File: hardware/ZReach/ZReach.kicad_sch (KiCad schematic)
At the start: 54 parts, among them J1 USB_C_Receptacle_USB2.0, J2 Conn_02x05_Odd_Even, J3 SMA, J4 NM, J5 Qwiic_RA, J6 Conn_01x02, J7 Conn_01x05, J8 Conn_01x05, SW1 PTS810, U1 CP2102N-Axx-xQFN20, U2 EFR32xG23-QFN48, U3 AP2127K-3.3, Y1 39MHz 10ppm, Y2 32768Hz

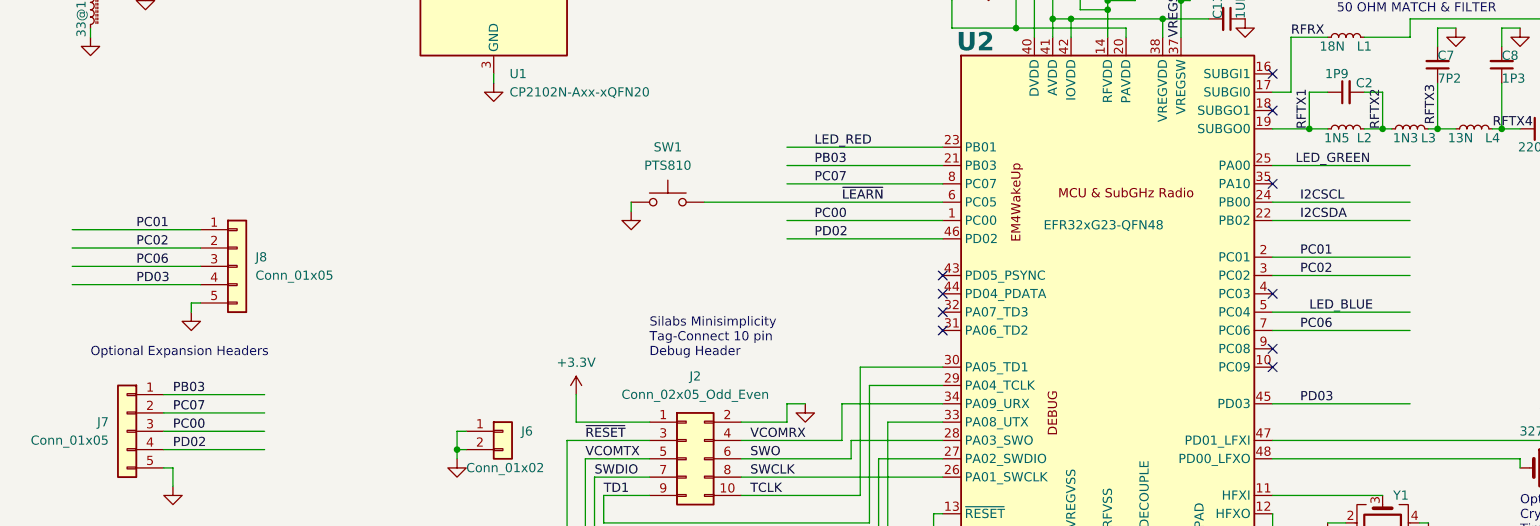
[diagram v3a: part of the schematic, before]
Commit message: PCB Layout DRC clean but needs more cleanup
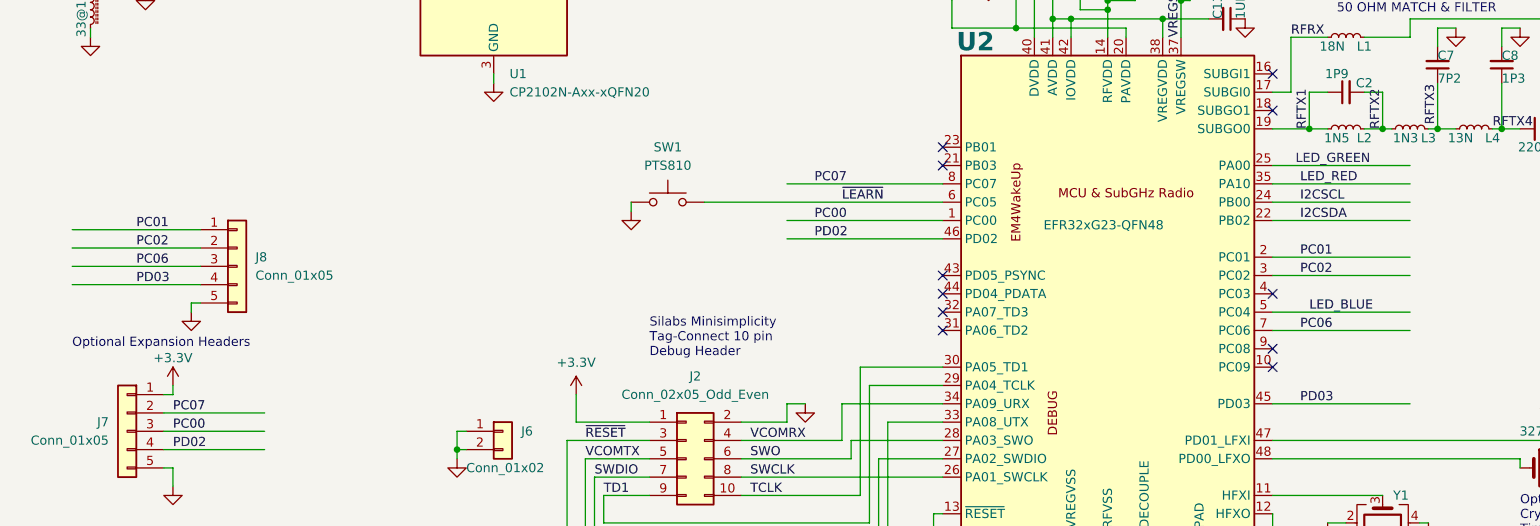
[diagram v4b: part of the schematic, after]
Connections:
- net +3.3V: now also J7.1 (Pin_1)
- net LED_RED: now also U2.35 (PA10); no longer U2.23 (PB01)
- net PB03: no longer names the net of U2.21 (PB03)
- net PB03: no longer J7.1 (Pin_1)
- no-connect marks 21 -> 22
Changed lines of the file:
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@@
   (no_connect (at 53.34 66.04))
   (no_connect (at 99.06 45.72))
+  (no_connect (at 148.59 99.06))
   (no_connect (at 148.59 121.92))
-  (no_connect (at 194.31 104.14))
   (no_connect (at 148.59 119.38))
   (no_connect (at 99.06 60.96))
@@
   (no_connect (at 99.06 73.66))
   (no_connect (at 148.59 116.84))
+  (no_connect (at 148.59 101.6))
   (no_connect (at 194.31 93.98))
   (no_connect (at 99.06 76.2))
@@
     (stroke (width 0) (type default))
   )
-  (wire (pts (xy 127 99.06) (xy 148.59 99.06))
-    (stroke (width 0) (type default))
-  )
   (wire (pts (xy 201.93 151.13) (xy 204.47 151.13))
     (stroke (width 0) (type default))
   )
-  (wire (pts (xy 127 101.6) (xy 148.59 101.6))
-    (stroke (width 0) (type default))
-  )
   (wire (pts (xy 35.56 176.53) (xy 33.02 176.53))
     (stroke (width 0) (type default))
@@
     (stroke (width 0) (type default))
   )
-  (wire (pts (xy 40.64 133.35) (xy 54.61 133.35))
-    (stroke (width 0) (type default))
-  )
   (wire (pts (xy 226.06 90.17) (xy 226.06 96.52))
     (stroke (width 0) (type default))
@@
     (stroke (width 0) (type default))
   )
+  (wire (pts (xy 41.91 133.35) (xy 41.91 132.08))
+    (stroke (width 0) (type default))
+  )
   (wire (pts (xy 90.17 21.59) (xy 86.36 21.59))
     (stroke (width 0) (type default))
@@
     (stroke (width 0) (type default))
   )
+  (wire (pts (xy 40.64 133.35) (xy 41.91 133.35))
+    (stroke (width 0) (type default))
+  )
   (wire (pts (xy 63.5 71.12) (xy 63.5 72.39))
     (stroke (width 0) (type default))
@@
   )
   (wire (pts (xy 196.85 83.82) (xy 196.85 91.44))
+    (stroke (width 0) (type default))
+  )
+  (wire (pts (xy 194.31 104.14) (xy 213.36 104.14))
     (stroke (width 0) (type default))
   )
@@
     (effects (font (size 1.27 1.27)) (justify left bottom))
   )
-  (text "Optional Expansion Headers" (at 30.48 128.27 0)
+  (text "Optional Expansion Headers" (at 27.94 127 0)
     (effects (font (size 1.27 1.27)) (justify left bottom))
   )
@@
     (effects (font (size 1.27 1.27)) (justify left bottom))
   )
-  (label "LED_RED" (at 130.81 99.06 0) (fields_autoplaced)
+  (label "LED_RED" (at 198.12 104.14 0) (fields_autoplaced)
     (effects (font (size 1.27 1.27)) (justify left bottom))
   )
@@
     (effects (font (size 1.27 1.27)) (justify left bottom))
   )
-  (label "PB03" (at 130.81 101.6 0) (fields_autoplaced)
-    (effects (font (size 1.27 1.27)) (justify left bottom))
-  )
   (label "SWDIO" (at 100.33 144.78 0) (fields_autoplaced)
     (effects (font (size 1.27 1.27)) (justify left bottom))
   )
   (label "I2CSCL" (at 198.12 106.68 0) (fields_autoplaced)
-    (effects (font (size 1.27 1.27)) (justify left bottom))
-  )
-  (label "PB03" (at 41.91 133.35 0) (fields_autoplaced)
     (effects (font (size 1.27 1.27)) (justify left bottom))
   )
@@
         )
       )
+    )
+  )
+  (symbol (lib_name "+3.3V_4") (lib_id "power:+3.3V") (at 41.91 132.08 0) (unit 1)
+    (in_bom yes) (on_board yes) (dnp no)
+    (property "Reference" "#PWR042" (at 41.91 135.89 0)
+      (effects (font (size 1.27 1.27)) hide)
+    )
+    (property "Value" "+3.3V" (at 41.91 128.27 0)
+      (effects (font (size 1.27 1.27)))
+    )
+    (property "Footprint" "" (at 41.91 132.08 0)
+      (effects (font (size 1.27 1.27)) hide)
+    )
+    (property "Datasheet" "" (at 41.91 132.08 0)
+      (effects (font (size 1.27 1.27)) hide)
+    )
+    (pin "1")
+    (instances
+      (project "ZReach"
+        (path "/ba492aef-b6eb-4439-8867-b040ec48a543"
+          (reference "#PWR042") (unit 1)
+        )
+      )

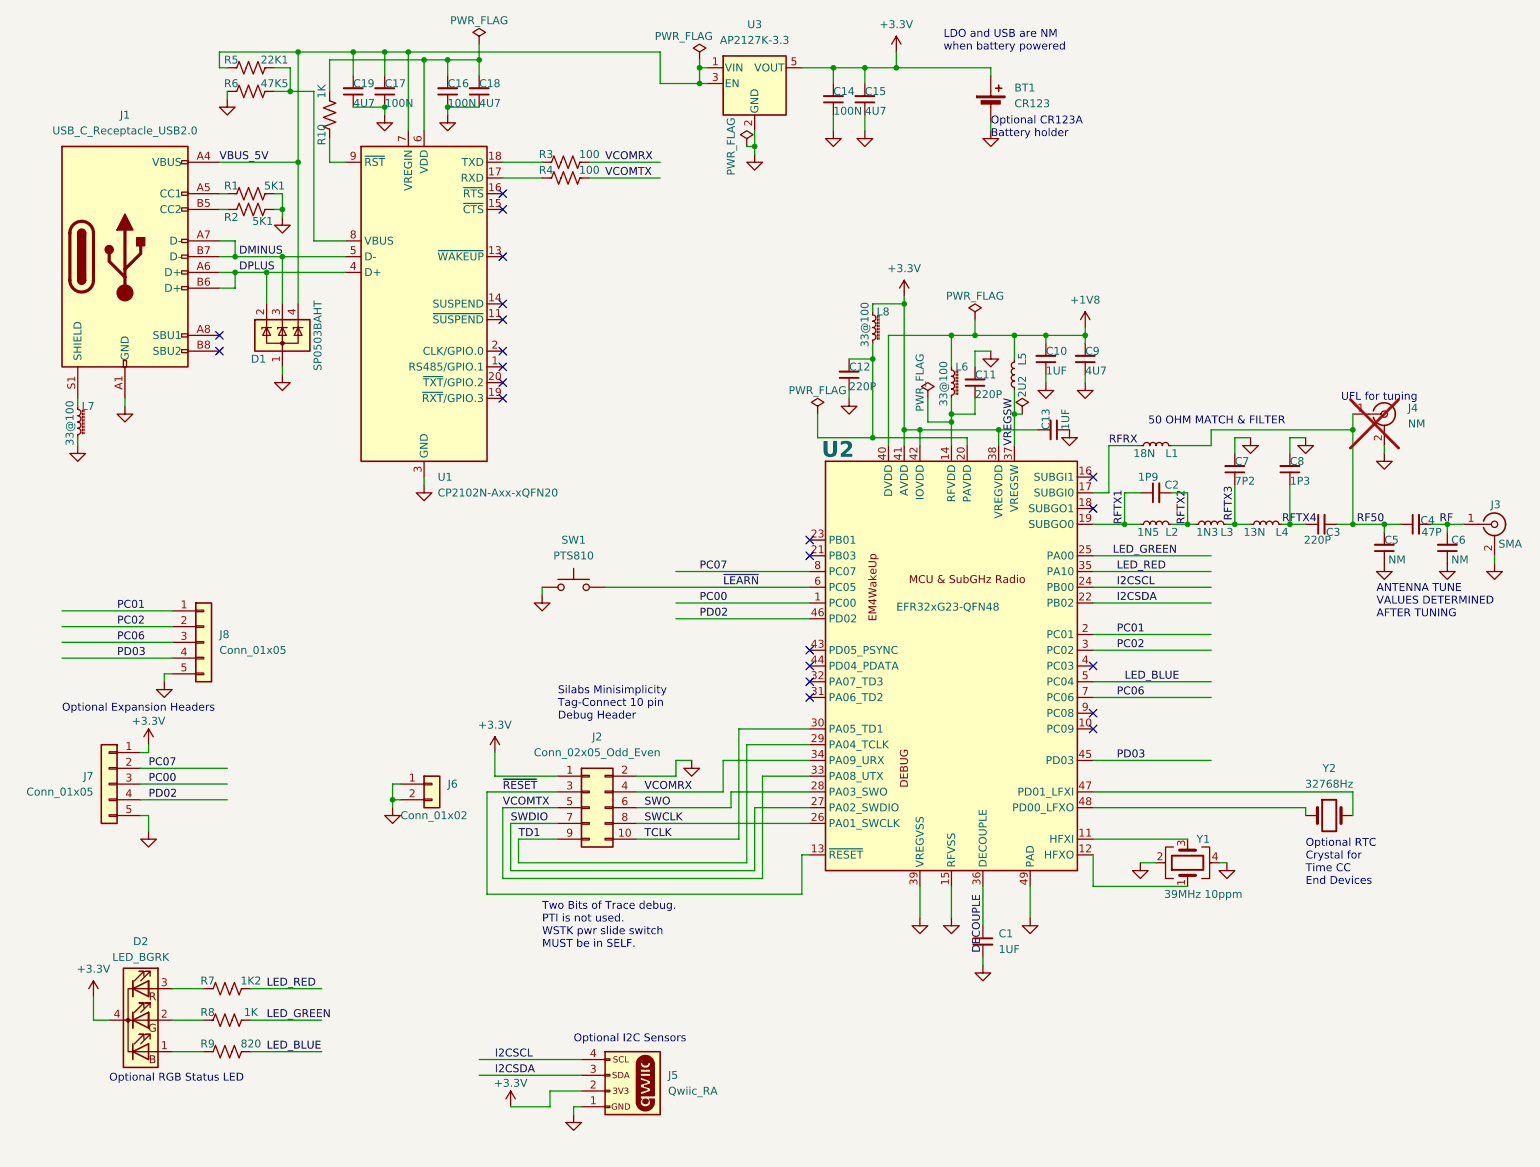
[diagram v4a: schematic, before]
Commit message: Update ZG23 symbol to the official one in the KiCAD library. Updated to KiCAD to V8.0
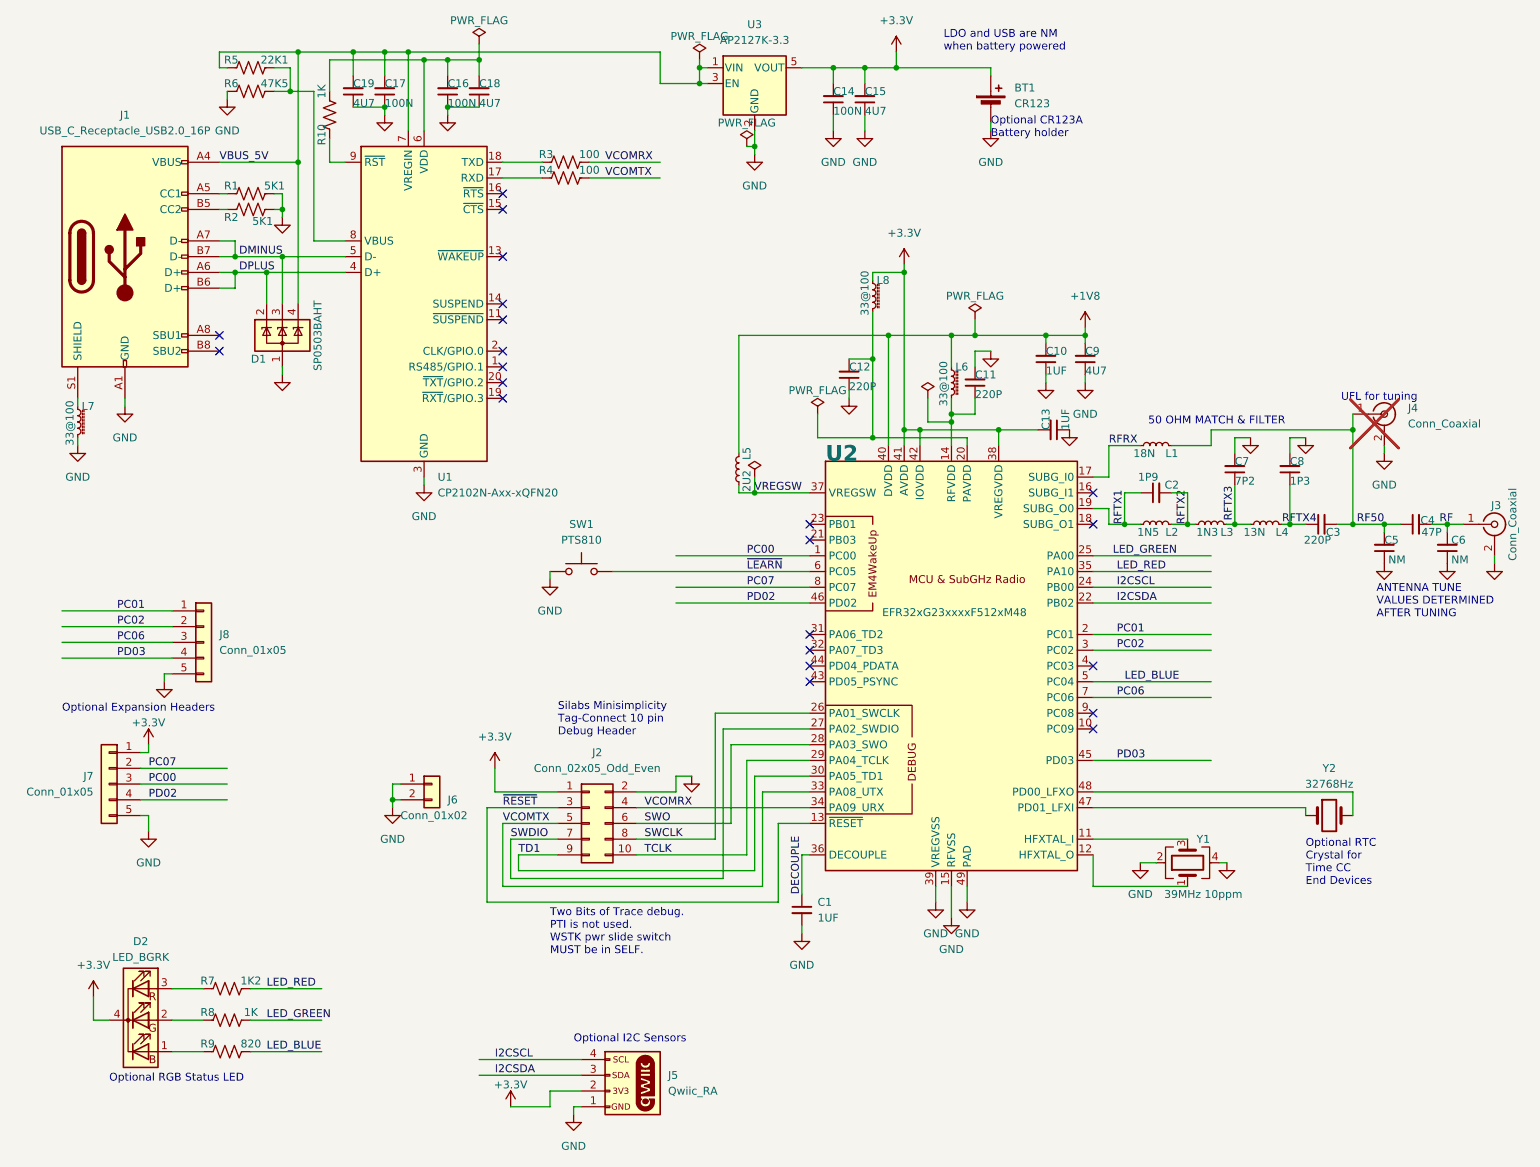
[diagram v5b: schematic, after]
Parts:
- removed U2: EFR32xG23-QFN48, Package_DFN_QFN:VQFN-48-1EP_6x6mm_P0.4mm_EP4.1x4.1mm, symbol MCU_Silabs:EFR32xG23-QFN48
- added U2: EFR32xG23xxxxF512xM48, Package_DFN_QFN:QFN-48-1EP_6x6mm_P0.4mm_EP4.3x4.3mm, symbol MCU_SiliconLabs:EFR32xG23xxxxF512xM48
- J1: value USB_C_Receptacle_USB2.0 -> USB_C_Receptacle_USB2.0_16P; symbol Connector:USB_C_Receptacle_USB2.0 -> Connector:USB_C_Receptacle_USB2.0_16P
- J3: value SMA -> Conn_Coaxial
- J4: value NM -> Conn_Coaxial; now in the parts list
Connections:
- net +1V8: now also U2.40 (DVDD)
- net +3.3V: now also U2.38 (VREGVDD), U2.41 (AVDD), U2.42 (IOVDD)
- net DECOUPLE: now also U2.36 (DECOUPLE)
- net GND: now also U2.15 (RFVSS), U2.39 (VREGVSS), U2.49 (PAD)
- net I2CSCL: now also U2.24 (PB00)
- net I2CSDA: now also U2.22 (PB02)
- net LED_BLUE: now also U2.5 (PC04)
- net LED_GREEN: now also U2.25 (PA00)
- net LED_RED: now also U2.35 (PA10)
- net PC00: now also U2.1 (PC00)
- net PC01: now also U2.2 (PC01)
- net PC02: now also U2.3 (PC02)
- net PC06: now also U2.7 (PC06)
- net PC07: now also U2.8 (PC07)
- net PD02: now also U2.46 (PD02)
- net PD03: now also U2.45 (PD03)
- net RFRX: now also U2.17 (SUBG_I0)
- net RFTX1: now also U2.19 (SUBG_O0)
- net SWCLK: now also U2.26 (PA01_SWCLK)
- net SWDIO: now also U2.27 (PA02_SWDIO)
- net SWO: now also U2.28 (PA03_SWO)
- net TCLK: now also U2.29 (PA04_TCLK)
- net TD1: now also U2.30 (PA05_TD1)
- net VCOMRX: now also U2.34 (PA09_URX)
- net VCOMTX: now also U2.33 (PA08_UTX)
- net VREGSW: now also U2.37 (VREGSW)
- net ~{LEARN}: now also U2.6 (PC05)
- net ~{RESET}: now also U2.13 (~{RESET})
- net at Y1.1: now also U2.12 (HFXTAL_O)
- net at Y1.3: now also U2.11 (HFXTAL_I)
- net at C12.2, L8.2: now also U2.20 (PAVDD)
- net at C11.1, L6.2: now also U2.14 (RFVDD)
- net at Y2.2: now also U2.48 (PD00_LFXO)
- net at Y2.1: now also U2.47 (PD01_LFXI)
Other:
- moved on the sheet: C1, J2, L5, L8, SW1

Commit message: Ordered components for initial build
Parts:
- C11, C12: footprint Capacitor_SMD:C_0603_1608Metric -> Capacitor_SMD:C_0402_1005Metric
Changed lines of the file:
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@@
 					(size 1.27 1.27)
 				)
+				(hide yes)
 			)
 		)
@@
 					(size 1.27 1.27)
 				)
+				(hide yes)
 			)
 		)
@@
 			)
 		)
-		(property "Footprint" "Capacitor_SMD:C_0603_1608Metric"
+		(property "Footprint" "Capacitor_SMD:C_0402_1005Metric"
 			(at 175.26 73.66 0)
 			(effects
@@
 			)
 		)
-		(property "Footprint" "Capacitor_SMD:C_0603_1608Metric"
+		(property "Footprint" "Capacitor_SMD:C_0402_1005Metric"
 			(at 154.94 72.39 0)
 			(effects

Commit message: Rev B PCB release
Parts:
- removed U1: CP2102N-Axx-xQFN20, Package_DFN_QFN:SiliconLabs_QFN-20-1EP_3x3mm_P0.5mm_EP1.8x1.8mm, symbol Interface_USB:CP2102N-Axx-xQFN20
- added SW2: PTS810, Button_Switch_SMD:SW_SPST_PTS810, symbol Switch:SW_Push
- added U3: CP2102N-Axx-xQFN24, Package_DFN_QFN:QFN-24-1EP_4x4mm_P0.5mm_EP2.6x2.6mm, symbol Interface_USB:CP2102N-Axx-xQFN24
- D1: renamed from D2; value LED_BGRK -> QLSP14RGB_B; footprint LED_SMD:LED_WS2812B-2020_PLCC4_2.0x2.0mm -> ZReach:LED_QLSP14RGB; symbol Device:LED_BGRK -> Device:LED_GRAB
- J1: renamed from J5; footprint ZReach:JST_PTH-4 -> Connector_JST:JST_SH_SM04B-SRSS-TB_1x04-1MP_P1.00mm_Horizontal
- renumbered C5 to C1, C6 to C10, C14 to C11, C15 to C12, C18 to C13, C19 to C14, C13 to C15, C17 to C16, C9 to C17, C10 to C18, C16 to C19, C12 to C2, C11 to C3, C8 to C5, C1 to C6, C3 to C7, C7 to C8, C2 to C9, D1 to D2, J3 to J2, J2 to J3, J7 to J5, J8 to J7, J1 to J8, L8 to L1, L3 to L2, L4 to L3, L2 to L4, L6 to L5, L1 to L6, L5 to L7, L7 to L8, R9 to R1, R1 to R10, R7 to R2, R8 to R3, R3 to R4, R4 to R5, R5 to R7, R2 to R8, R10 to R9, U2 to U1, U3 to U2, Y2 to Y1, Y1 to Y2
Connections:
- net +3.3V: now also D1.3 (A); no longer D1.4 (K)
- net DMINUS: now also U3.4 (D-)
- net DPLUS: now also U3.3 (D+)
- net GND: now also SW2.1, U3.2 (GND), U3.25 (GND)
- net VBUS_5V: now also U3.7 (VREGIN)
- net ~{RESET}: now also SW2.2
- net at R2.1: now also D1.4 (BK); no longer D1.3 (RA)
- net at R1.1: now also D1.2 (RK); no longer D1.1 (BA)
- net at R3.1: now also D1.1 (GK); no longer D1.2 (GA)
- net at R5.1: now also U3.20 (RXD)
- net at R4.1: now also U3.21 (TXD)
- net at C13.2, C19.2, R9.2: now also U3.5 (VIO), U3.6 (VDD)
- net at R6.2, R7.2: now also U3.8 (VBUS)
- net at R9.1: now also U3.9 (~{RST})
- no-connect marks 22 -> 25
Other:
- note added: "NM"
- note added: "Two Bits of Trace debug. PTI is not used."
- note removed: "Two Bits of Trace debug. PTI is not used. WSTK pwr slide switch MUST be in SELF."
- moved on the sheet: C13, C19, D1
